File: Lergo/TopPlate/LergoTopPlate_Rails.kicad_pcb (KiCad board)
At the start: 2 copper layers, 164 x 146.3 mm, 33 parts, among them SW2 KEY_SWITCH, SW2 PRO MICRO

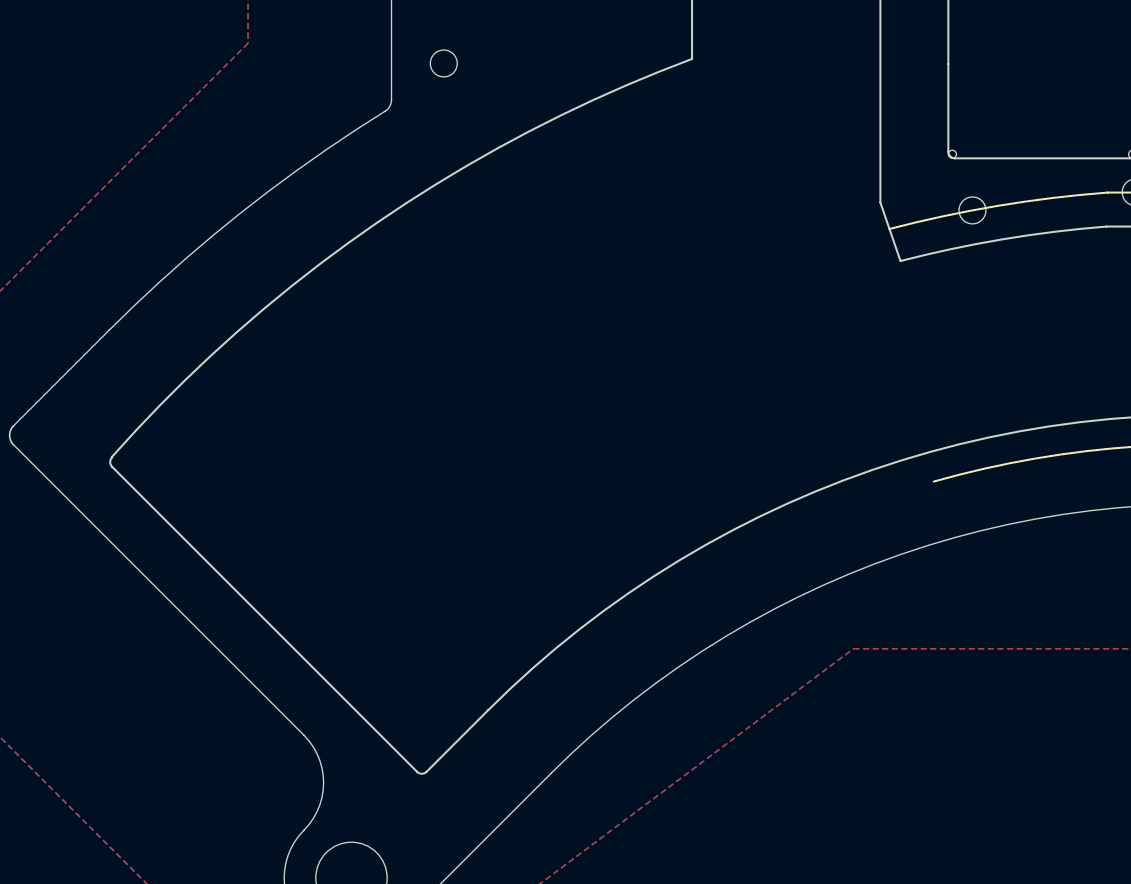
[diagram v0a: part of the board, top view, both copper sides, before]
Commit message: Integrating Pimoroni trackball in all top plates.
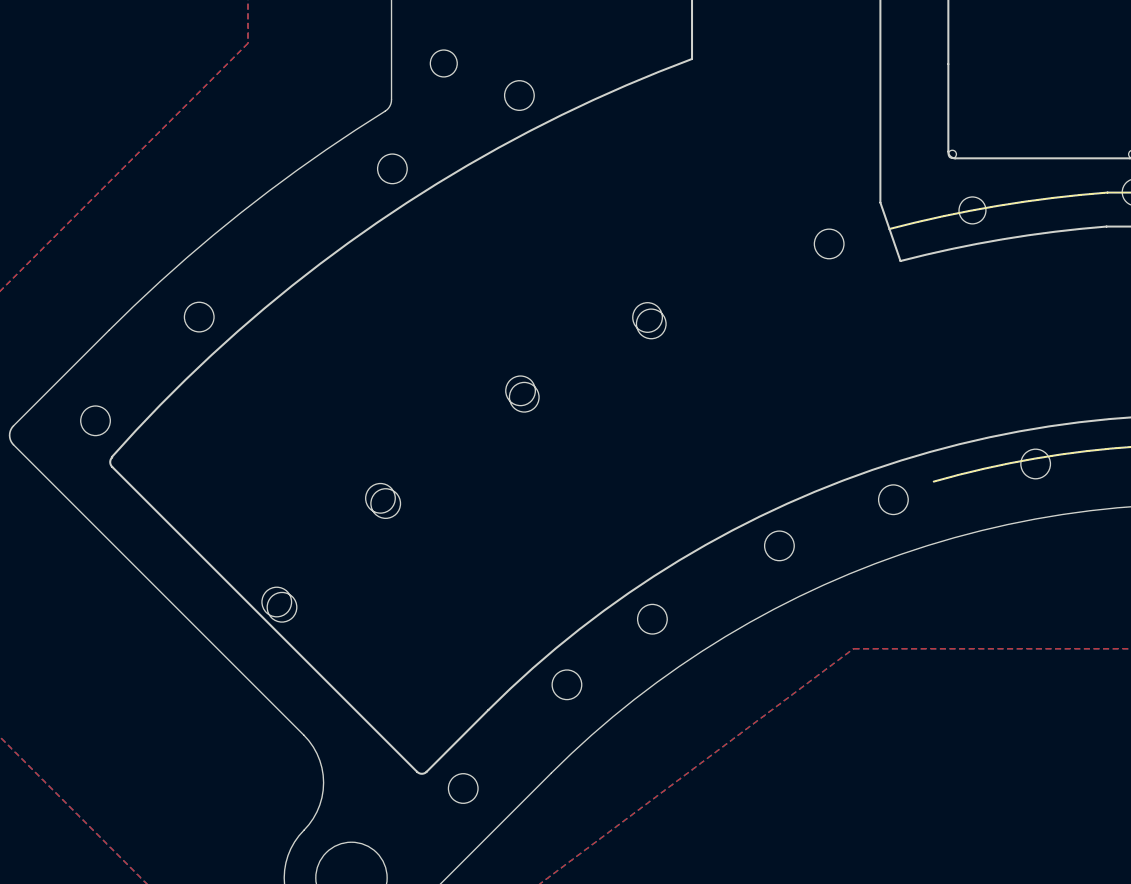
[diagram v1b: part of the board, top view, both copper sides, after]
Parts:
- added REF**: Pimoroni_Trackball, Lergo Footprints:Pimoroni_Trackball, F.Cu at (141.8, 120.6)
- added REF**: Pimoroni_Trackball, Lergo Footprints:Pimoroni_Trackball, F.Cu at (120.8, 129.1)
- added REF**: Pimoroni_Trackball, Lergo Footprints:Pimoroni_Trackball, F.Cu at (103.9, 142.1)
- added REF**: Pimoroni_Trackball, Lergo Footprints:Pimoroni_Trackball, F.Cu at (90.4, 128.6)
- added REF**: Pimoroni_Trackball, Lergo Footprints:Pimoroni_Trackball, F.Cu at (111.3, 112.6)

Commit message: Lergo V1.A, ready for first prototype run
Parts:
- SW2: footprint Lergo Footprints:CherryMX_Lergo_v1_TopPlate_2u_1u_Rail_Helper -> Lergo Footprints:CherryMX_Lergo_v1_TopPlate_2u_1u_Rail_End
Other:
- outline, holes or cut-outs redrawn
